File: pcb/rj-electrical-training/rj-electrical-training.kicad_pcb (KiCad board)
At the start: 4 copper layers, 100 x 40 mm, 65 parts, among them J1 USB_C_Receptacle_USB2.0_16P, J2 SWD, SW1 PTS810, SW2 PTS810, SW3 PTS810, SW4 PTS810, U1 RP2040, U2 W25Q16JVSS, U3 AP2112K-3.3, U4 USBLC6-2P6, U5 USBLC6-2P6, U6 LSM6DSM, Y1 ABM8-272-T3

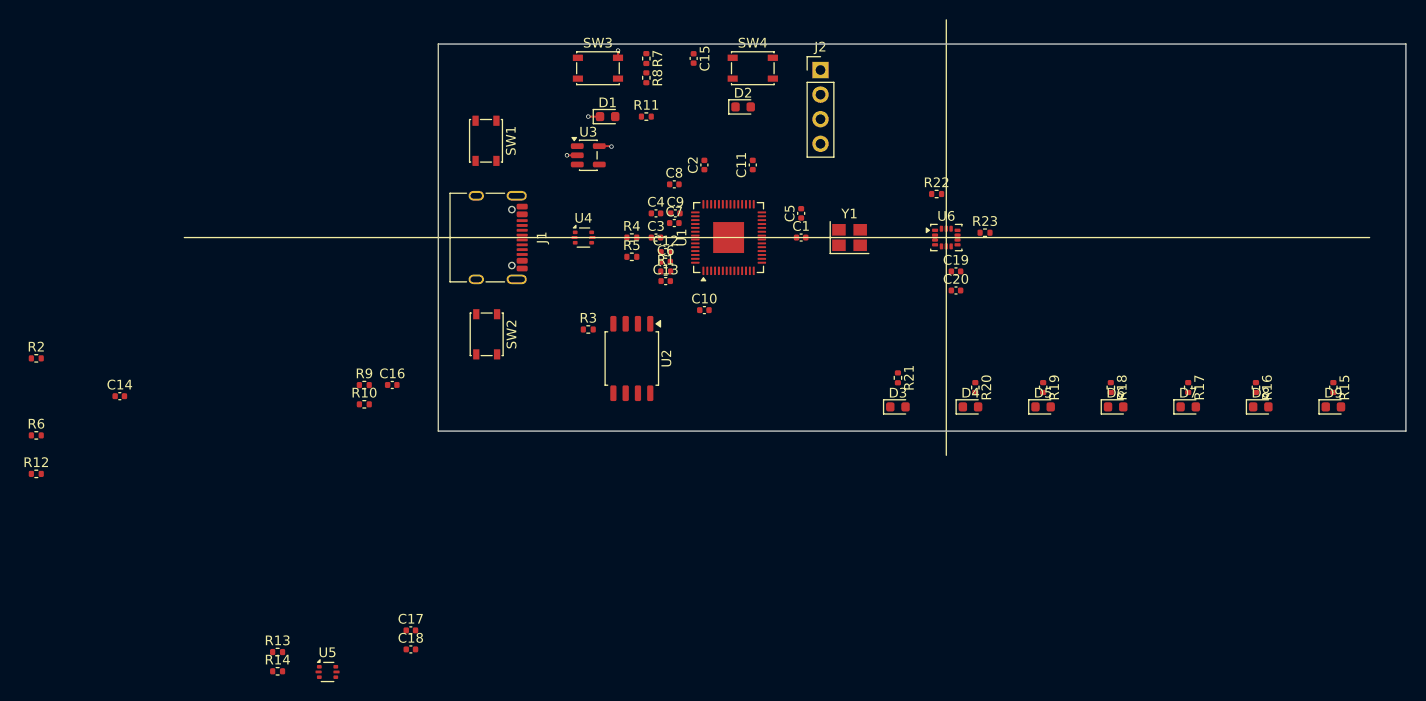
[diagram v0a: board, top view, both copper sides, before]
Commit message: Added SPI buses so slave master protocols work
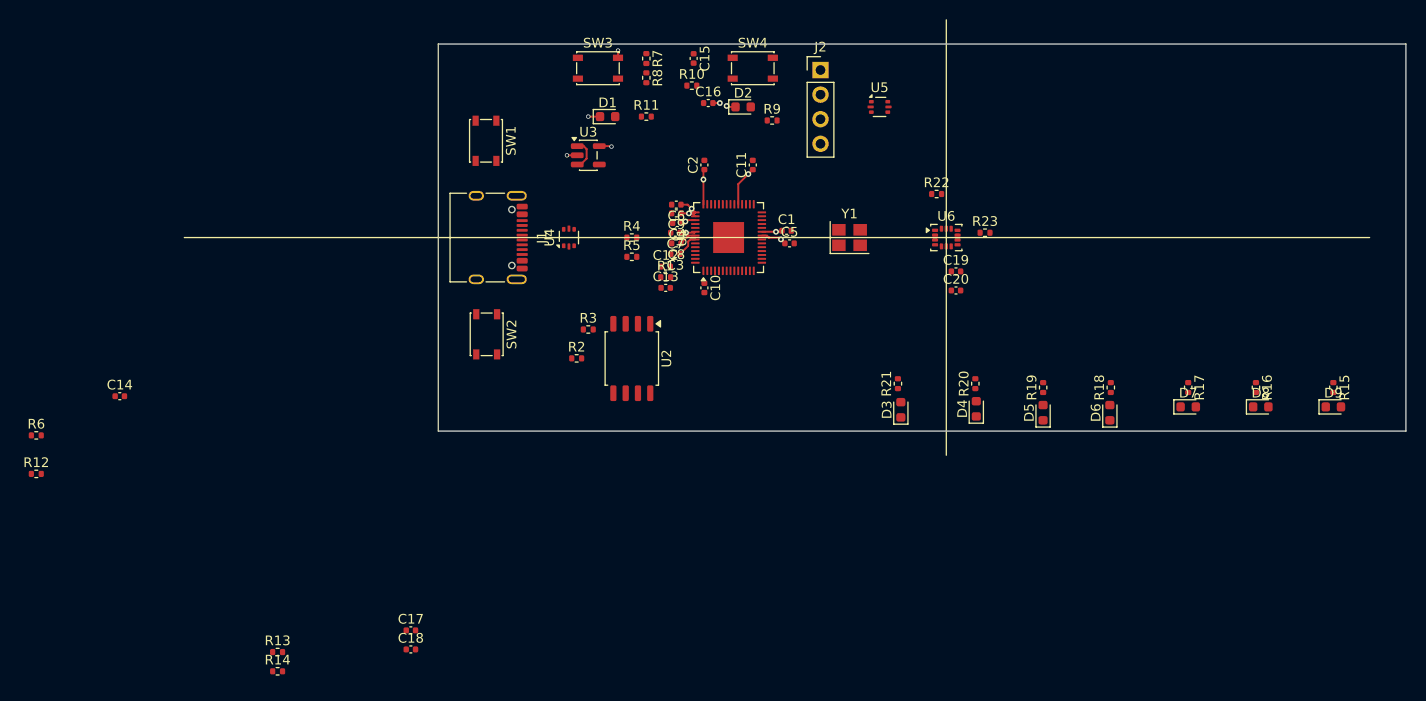
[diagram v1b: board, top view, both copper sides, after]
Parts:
- moved U5 81.6 mm to (208.1, 44.0)
- moved R2 55.8 mm to (176.8, 70.0)
- moved R9 50.2 mm to (197.0, 45.4)
- moved R10 47.2 mm to (188.7, 41.8)
- moved C16 43.8 mm to (190.4, 43.6)
- moved C8 6.10 mm to (187.1, 58.1), turned to 180 degrees
- moved C6 6.00 mm to (187.1, 54.1), turned to 180 degrees
- moved C5 3.32 mm to (198.8, 58.1), turned to 0 degrees
- moved C3 2.62 mm to (187.0, 59.2), turned to 180 degrees
- moved C4 2.42 mm to (187.2, 56.0), turned to 180 degrees
- moved C10 2.30 mm to (190.0, 62.7), turned to -90 degrees
- moved C1 1.66 mm to (198.5, 56.8)
- moved C12 1.50 mm to (186.0, 60.5)
- moved U4 1.50 mm to (176.0, 57.5), turned to 90 degrees
- moved C7 1.01 mm to (187.0, 57.0), turned to 180 degrees
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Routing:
- net +3.3V: track 2.14 -> 19.8 mm, vias 2 -> 8
- net +1.1V: track 0.00 -> 5.90 mm, vias 0 -> 2
- net VBUS: track 0.00 -> 3.29 mm
- net GND: track 2.28 -> 3.95 mm, vias 2 -> 4
